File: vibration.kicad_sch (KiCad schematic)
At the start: 5 parts, among them J6 Conn_01x02, Q3 SS8050

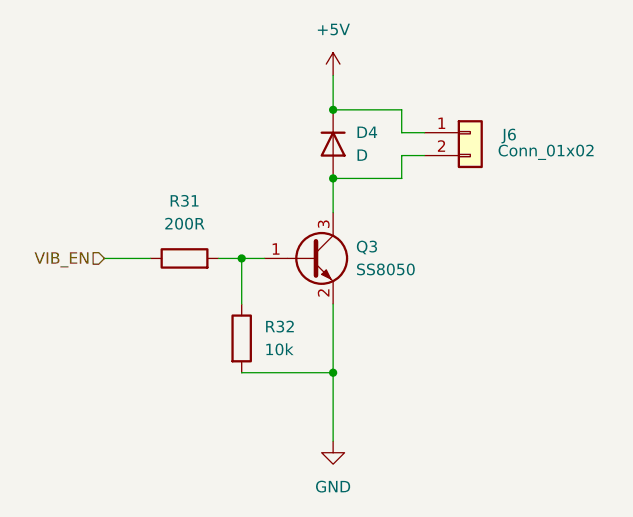
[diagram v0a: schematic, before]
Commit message: add SD card
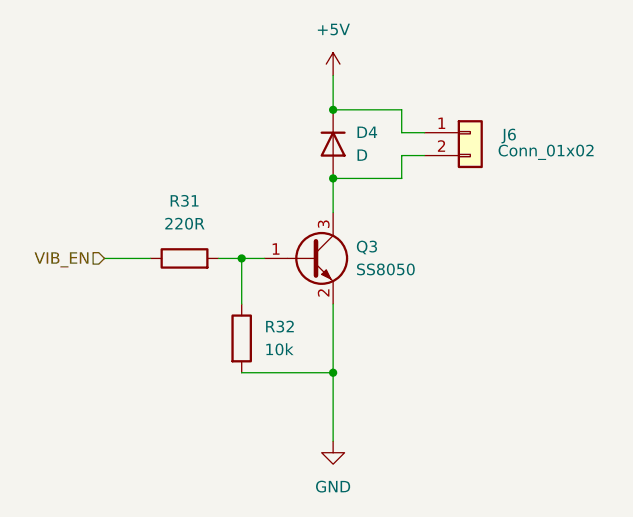
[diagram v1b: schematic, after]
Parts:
- D4: footprint (none) -> Diode_SMD:D_SMA; LCSC (none) -> C64982; Manufacturer (none) -> MDD(Microdiode Semiconductor); Manufacturer Part Number (none) -> B340A
- R31: value 200R -> 220R; footprint (none) -> Resistor_SMD:R_0603_1608Metric
- R32: footprint (none) -> Resistor_SMD:R_0603_1608Metric
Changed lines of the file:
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@@
 			)
 		)
-		(property "Footprint" ""
+		(property "Footprint" "Diode_SMD:D_SMA"
 			(at 132.08 74.93 0)
 			(effects
@@
 		)
 		(property "Sim.Pins" "1=K 2=A"
+			(at 132.08 74.93 0)
+			(effects
+				(font
+					(size 1.27 1.27)
+				)
+				(hide yes)
+			)
+		)
+		(property "LCSC" "C64982"
+			(at 132.08 74.93 0)
+			(effects
+				(font
+					(size 1.27 1.27)
+				)
+				(hide yes)
+			)
+		)
+		(property "Manufacturer" "MDD(Microdiode Semiconductor)"
+			(at 132.08 74.93 0)
+			(effects
+				(font
+					(size 1.27 1.27)
+				)
+				(hide yes)
+			)
+		)
+		(property "Manufacturer Part Number" "B340A"
 			(at 132.08 74.93 0)
 			(effects
@@
 			)
 		)
-		(property "Footprint" ""
+		(property "Footprint" "Resistor_SMD:R_0603_1608Metric"
 			(at 120.142 96.52 90)
 			(effects
@@
 			)
 		)
-		(property "Value" "200R"
+		(property "Value" "220R"
 			(at 115.57 83.82 90)
 			(effects
@@
 			)
 		)
-		(property "Footprint" ""
+		(property "Footprint" "Resistor_SMD:R_0603_1608Metric"
 			(at 115.57 89.408 90)
 			(effects

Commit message: small updates in component selection
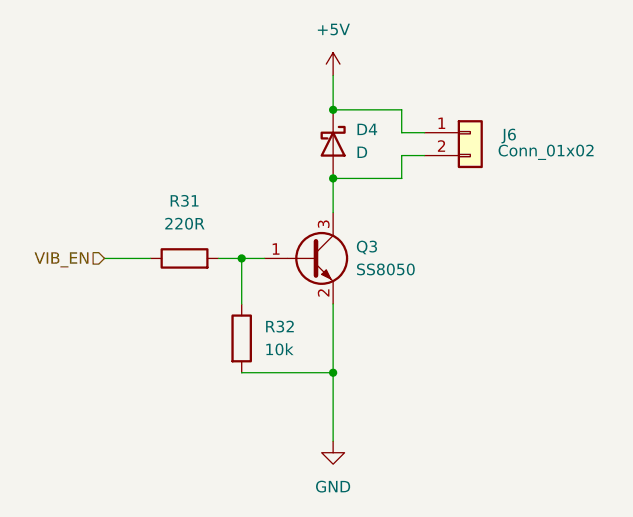
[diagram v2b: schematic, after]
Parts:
- D4: symbol Device:D -> Device:D_Schottky
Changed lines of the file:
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@@
 	)
 	(symbol
-		(lib_id "Device:D")
+		(lib_id "Device:D_Schottky")
 		(at 132.08 74.93 270)
 		(unit 1)
@@
 		(fields_autoplaced yes)
 		(property "Reference" "D4"
-			(at 134.62 73.6599 90)
+			(at 134.62 73.3424 90)
 			(effects
 				(font
@@
 		)
 		(property "Value" "D"
-			(at 134.62 76.1999 90)
+			(at 134.62 75.8824 90)
 			(effects
 				(font
@@
 			)
 		)
-		(property "Description" "Diode"
+		(property "Description" "Schottky diode"
 			(at 132.08 74.93 0)
 			(effects

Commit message: fix usb and add esd diodes, some other checks
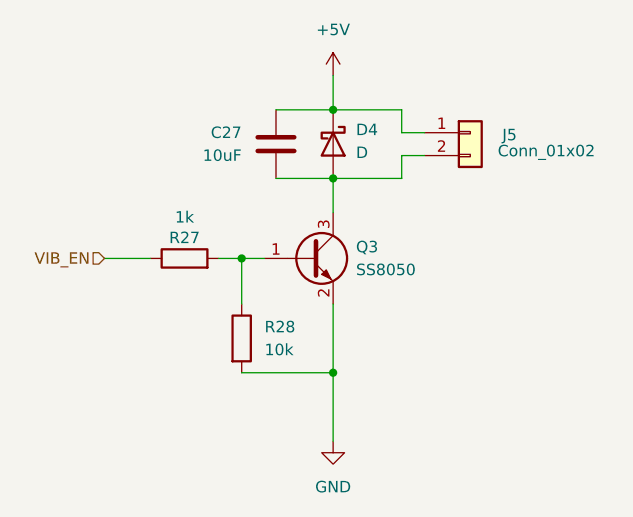
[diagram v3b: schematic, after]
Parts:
- removed R31: 220R, Resistor_SMD:R_0603_1608Metric, symbol Device:R
- added C27: 10uF, Capacitor_SMD:C_0603_1608Metric, symbol Device:C
- added R27: 1k, Resistor_SMD:R_0402_1005Metric, symbol Device:R
- renumbered J6 to J5, R32 to R28
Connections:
- net +5V: now also C27.1
- net VIB_EN: now also R27.1
- net at D4.2 (A), J5.2 (Pin_2), Q3.3 (C): now also C27.2
- net at Q3.1 (B), R28.1: now also R27.2
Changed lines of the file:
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@@
+	(wire
+		(pts
+			(xy 125.73 78.74) (xy 132.08 78.74)
+		)
+		(stroke
+			(width 0)
+			(type default)
+		)
+	)
 	(wire
 		(pts
@@
 		(pts
 			(xy 132.08 100.33) (xy 132.08 92.71)
+		)
+		(stroke
+			(width 0)
+			(type default)
+		)
+	)
+	(wire
+		(pts
+			(xy 125.73 71.12) (xy 132.08 71.12)
 		)
 		(stroke
@@
 		(on_board yes)
 		(dnp no)
-		(property "Reference" "J6"
+		(property "Reference" "J5"
 			(at 150.876 73.914 0)
 			(effects
@@
 			(project "gameboy"
 				(path "/f4643692-c319-40a7-82a2-3e775c0a417f/fa61dece-89ff-456c-a30f-6bfd2f1cc11c"
-					(reference "J6")
+					(reference "J5")
 					(unit 1)
 				)
@@
 	)
 	(symbol
+		(lib_id "Device:R")
+		(at 115.57 87.63 90)
+		(unit 1)
+		(exclude_from_sim no)
+		(in_bom yes)
+		(on_board yes)
+		(dnp no)
+		(property "Reference" "R27"
+			(at 115.57 85.344 90)
+			(effects
+				(font
+					(size 1.27 1.27)
+				)
+			)
+		)
+		(property "Value" "1k"
+			(at 115.57 83.058 90)
+			(effects
+				(font
+					(size 1.27 1.27)
+				)
+			)
+		)
+		(property "Footprint" "Resistor_SMD:R_0402_1005Metric"
+			(at 115.57 89.408 90)
+			(effects
+				(font
+					(size 1.27 1.27)
+				)
+				(hide yes)
+			)
+		)
+		(property "Datasheet" "~"
+			(at 115.57 87.63 0)
+			(effects
+				(font
+					(size 1.27 1.27)
+				)
+				(hide yes)
+			)
+		)
+		(property "Description" ""
+			(at 115.57 87.63 0)
+			(effects
+				(font
+					(size 1.27 1.27)
+				)
+			)
+		)
+		(pin "1"
+		)
+		(pin "2"
+		)
+		(instances
+			(project "gameboy"
+				(path "/f4643692-c319-40a7-82a2-3e775c0a417f/fa61dece-89ff-456c-a30f-6bfd2f1cc11c"
+					(reference "R27")
+					(unit 1)
+				)
+			)
+		)
+	)
+	(symbol
 		(lib_id "power:+5V")
 		(at 132.08 67.31 0)
@@
 		(dnp no)
 		(fields_autoplaced yes)
-		(property "Reference" "#PWR034"
+		(property "Reference" "#PWR033"
 			(at 132.08 71.12 0)
 			(effects
@@
 			(project ""
 				(path "/f4643692-c319-40a7-82a2-3e775c0a417f/fa61dece-89ff-456c-a30f-6bfd2f1cc11c"
-					(reference "#PWR034")
+					(reference "#PWR033")
+					(unit 1)
+				)
+			)
+		)
+	)
+	(symbol
+		(lib_id "Device:C")
+		(at 125.73 74.93 0)
+		(mirror y)
+		(unit 1)
+		(exclude_from_sim no)
+		(in_bom yes)
+		(on_board yes)
+		(dnp no)
+		(property "Reference" "C27"
+			(at 121.92 73.6599 0)
+			(effects
+				(font
+					(size 1.27 1.27)
+				)
+				(justify left)
+			)
+		)
+		(property "Value" "10uF"
+			(at 121.92 76.1999 0)
+			(effects
+				(font
+					(size 1.27 1.27)
+				)
+				(justify left)
+			)
+		)
+		(property "Footprint" "Capacitor_SMD:C_0603_1608Metric"
+			(at 124.7648 78.74 0)
+			(effects
+				(font
+					(size 1.27 1.27)
+				)
+				(hide yes)
+			)
+		)
+		(property "Datasheet" "~"
+			(at 125.73 74.93 0)
+			(effects
+				(font
+					(size 1.27 1.27)
+				)
+				(hide yes)
+			)
+		)
+		(property "Description" "Unpolarized capacitor"
+			(at 125.73 74.93 0)
+			(effects
+				(font
+					(size 1.27 1.27)
+				)
+				(hide yes)
+			)
+		)
+		(property "LCSC" ""
+			(at 125.73 74.93 0)
+			(effects
+				(font
+					(size 1.27 1.27)
+				)
+				(hide yes)
+			)
+		)
+		(property "Manufacturer" ""
+			(at 125.73 74.93 0)
+			(effects
+				(font
+					(size 1.27 1.27)
+				)
+				(hide yes)
+			)
+		)
+		(property "Manufacturer Part Number" ""
+			(at 125.73 74.93 0)
+			(effects
+				(font
+					(size 1.27 1.27)
+				)
+				(hide yes)
+			)
+		)
+		(pin "2"
+		)
+		(pin "1"
+		)
+		(instances
+			(project "gameboy"
+				(path "/f4643692-c319-40a7-82a2-3e775c0a417f/fa61dece-89ff-456c-a30f-6bfd2f1cc11c"
+					(reference "C27")
 					(unit 1)
 				)
@@
 		(dnp no)
 		(fields_autoplaced yes)
-		(property "Reference" "#PWR035"
+		(property "Reference" "#PWR034"
 			(at 132.08 114.3 0)
 			(effects
@@
 			(project ""
 				(path "/f4643692-c319-40a7-82a2-3e775c0a417f/fa61dece-89ff-456c-a30f-6bfd2f1cc11c"
-					(reference "#PWR035")
+					(reference "#PWR034")
 					(unit 1)
 				)
@@
 		(dnp no)
 		(fields_autoplaced yes)
-		(property "Reference" "R32"
+		(property "Reference" "R28"
 			(at 124.46 95.2499 0)
 			(effects
@@
 			(project ""
 				(path "/f4643692-c319-40a7-82a2-3e775c0a417f/fa61dece-89ff-456c-a30f-6bfd2f1cc11c"
-					(reference "R32")
+					(reference "R28")
 					(unit 1)
 				)
-			)
-		)
-	)
-	(symbol
-		(lib_id "Device:R")
-		(at 115.57 87.63 90)
-		(unit 1)
-		(exclude_from_sim no)
-		(in_bom yes)
-		(on_board yes)
-		(dnp no)
-		(fields_autoplaced yes)
-		(property "Reference" "R31"
-			(at 115.57 81.28 90)
-			(effects
-				(font
-					(size 1.27 1.27)
-				)
-			)
-		)
-		(property "Value" "220R"
-			(at 115.57 83.82 90)
-			(effects
-				(font
-					(size 1.27 1.27)
-				)
-			)
-		)
-		(property "Footprint" "Resistor_SMD:R_0603_1608Metric"
-			(at 115.57 89.408 90)
-			(effects
-				(font
-					(size 1.27 1.27)
-				)
-				(hide yes)
-			)
-		)
-		(property "Datasheet" "~"
-			(at 115.57 87.63 0)
-			(effects
-				(font
-					(size 1.27 1.27)
-				)
-				(hide yes)
-			)
-		)
-		(property "Description" "Resistor"
-			(at 115.57 87.63 0)
-			(effects
-				(font
-					(size 1.27 1.27)
-				)
-				(hide yes)
-			)
-		)
-		(property "LCSC" ""
-			(at 115.57 87.63 0)
-			(effects
-				(font
-					(size 1.27 1.27)
-				)
-				(hide yes)
-			)
-		)
-		(property "Manufacturer" ""
-			(at 115.57 87.63 0)
-			(effects
-				(font
-					(size 1.27 1.27)
-				)
-				(hide yes)
-			)
-		)
-		(property "Manufacturer Part Number" ""
-			(at 115.57 87.63 0)
-			(effects
-				(font
-					(size 1.27 1.27)
-				)
-				(hide yes)
-			)
-		)
-		(pin "1"
-		)
-		(pin "2"
-		)
-		(instances
-			(project ""
-				(path "/f4643692-c319-40a7-82a2-3e775c0a417f/fa61dece-89ff-456c-a30f-6bfd2f1cc11c"
-					(reference "R31")
-					(unit 1)
-				)

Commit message: whole bunch of layout done
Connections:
- net +5V renamed VDC
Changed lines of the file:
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@@
-	)
-	(symbol
-		(lib_id "power:+5V")
-		(at 132.08 67.31 0)
-		(unit 1)
-		(exclude_from_sim no)
-		(in_bom yes)
-		(on_board yes)
-		(dnp no)
-		(fields_autoplaced yes)
-		(property "Reference" "#PWR033"
-			(at 132.08 71.12 0)
-			(effects
-				(font
-					(size 1.27 1.27)
-				)
-				(hide yes)
-			)
-		)
-		(property "Value" "+5V"
-			(at 132.08 62.23 0)
-			(effects
-				(font
-					(size 1.27 1.27)
-				)
-			)
-		)
-		(property "Footprint" ""
-			(at 132.08 67.31 0)
-			(effects
-				(font
-					(size 1.27 1.27)
-				)
-				(hide yes)
-			)
-		)
-		(property "Datasheet" ""
-			(at 132.08 67.31 0)
-			(effects
-				(font
-					(size 1.27 1.27)
-				)
-				(hide yes)
-			)
-		)
-		(property "Description" "Power symbol creates a global label with name \"+5V\""
-			(at 132.08 67.31 0)
-			(effects
-				(font
-					(size 1.27 1.27)
-				)
-				(hide yes)
-			)
-		)
-		(pin "1"
-		)
-		(instances
-			(project ""
-				(path "/f4643692-c319-40a7-82a2-3e775c0a417f/fa61dece-89ff-456c-a30f-6bfd2f1cc11c"
-					(reference "#PWR033")
-					(unit 1)
-				)
-			)
-		)
 	)
 	(symbol
@@
 					(unit 1)
 				)
+			)
+		)
+	)
+	(symbol
+		(lib_id "power:VDC")
+		(at 132.08 67.31 0)
+		(unit 1)
+		(exclude_from_sim no)
+		(in_bom yes)
+		(on_board yes)
+		(dnp no)
+		(fields_autoplaced yes)
+		(property "Reference" "#PWR026"
+			(at 132.08 71.12 0)
+			(effects
+				(font
+					(size 1.27 1.27)
+				)
+				(hide yes)
+			)
+		)
+		(property "Value" "VDC"
+			(at 132.08 62.23 0)
+			(effects
+				(font
+					(size 1.27 1.27)
+				)
+			)
+		)
+		(property "Footprint" ""
+			(at 132.08 67.31 0)
+			(effects
+				(font
+					(size 1.27 1.27)
+				)
+				(hide yes)
+			)
+		)
+		(property "Datasheet" ""
+			(at 132.08 67.31 0)
+			(effects
+				(font
+					(size 1.27 1.27)
+				)
+				(hide yes)
+			)
+		)
+		(property "Description" "Power symbol creates a global label with name \"VDC\""
+			(at 132.08 67.31 0)
+			(effects
+				(font
+					(size 1.27 1.27)
+				)
+				(hide yes)
+			)
+		)
+		(pin "1"
+		)
+		(instances
+			(project ""
+				(path "/f4643692-c319-40a7-82a2-3e775c0a417f/fa61dece-89ff-456c-a30f-6bfd2f1cc11c"
+					(reference "#PWR026")
+					(unit 1)
+				)

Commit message: more routing
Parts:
- J5: footprint Connector_JST:JST_PH_B2B-PH-K_1x02_P2.00mm_Vertical -> Connector_JST:JST_PH_S2B-PH-SM4-TB_1x02-1MP_P2.00mm_Horizontal; LCSC C131337 -> C295747; Manufacturer Part Number B2B-PH-K-S(LF)(SN) -> S2B-PH-SM4-TB(LF)(SN)
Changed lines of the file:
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@@
-	)
-	(symbol
-		(lib_id "Connector_Generic:Conn_01x02")
-		(at 147.32 73.66 0)
-		(unit 1)
-		(exclude_from_sim no)
-		(in_bom yes)
-		(on_board yes)
-		(dnp no)
-		(property "Reference" "J5"
-			(at 150.876 73.914 0)
-			(effects
-				(font
-					(size 1.27 1.27)
-				)
-				(justify left)
-			)
-		)
-		(property "Value" "Conn_01x02"
-			(at 150.368 75.692 0)
-			(effects
-				(font
-					(size 1.27 1.27)
-				)
-				(justify left)
-			)
-		)
-		(property "Footprint" "Connector_JST:JST_PH_B2B-PH-K_1x02_P2.00mm_Vertical"
-			(at 147.32 73.66 0)
-			(effects
-				(font
-					(size 1.27 1.27)
-				)
-				(hide yes)
-			)
-		)
-		(property "Datasheet" "~"
-			(at 147.32 73.66 0)
-			(effects
-				(font
-					(size 1.27 1.27)
-				)
-				(hide yes)
-			)
-		)
-		(property "Description" "Generic connector, single row, 01x02, script generated (kicad-library-utils/schlib/autogen/connector/)"
-			(at 147.32 73.66 0)
-			(effects
-				(font
-					(size 1.27 1.27)
-				)
-				(hide yes)
-			)
-		)
-		(property "LCSC" "C131337"
-			(at 147.32 73.66 0)
-			(effects
-				(font
-					(size 1.27 1.27)
-				)
-				(hide yes)
-			)
-		)
-		(property "Manufacturer" "JST"
-			(at 147.32 73.66 0)
-			(effects
-				(font
-					(size 1.27 1.27)
-				)
-				(hide yes)
-			)
-		)
-		(property "Manufacturer Part Number" "B2B-PH-K-S(LF)(SN)"
-			(at 147.32 73.66 0)
-			(effects
-				(font
-					(size 1.27 1.27)
-				)
-				(hide yes)
-			)
-		)
-		(pin "2"
-		)
-		(pin "1"
-		)
-		(instances
-			(project "gameboy"
-				(path "/f4643692-c319-40a7-82a2-3e775c0a417f/fa61dece-89ff-456c-a30f-6bfd2f1cc11c"
-					(reference "J5")
-					(unit 1)
-				)
-			)
-		)
 	)
 	(symbol
@@
 					(unit 1)
 				)
+			)
+		)
+	)
+	(symbol
+		(lib_id "Connector_Generic:Conn_01x02")
+		(at 147.32 73.66 0)
+		(unit 1)
+		(exclude_from_sim no)
+		(in_bom yes)
+		(on_board yes)
+		(dnp no)
+		(property "Reference" "J5"
+			(at 150.876 73.914 0)
+			(effects
+				(font
+					(size 1.27 1.27)
+				)
+				(justify left)
+			)
+		)
+		(property "Value" "Conn_01x02"
+			(at 150.368 75.692 0)
+			(effects
+				(font
+					(size 1.27 1.27)
+				)
+				(justify left)
+			)
+		)
+		(property "Footprint" "Connector_JST:JST_PH_S2B-PH-SM4-TB_1x02-1MP_P2.00mm_Horizontal"
+			(at 147.32 73.66 0)
+			(effects
+				(font
+					(size 1.27 1.27)
+				)
+				(hide yes)
+			)
+		)
+		(property "Datasheet" "~"
+			(at 147.32 73.66 0)
+			(effects
+				(font
+					(size 1.27 1.27)
+				)
+				(hide yes)
+			)
+		)
+		(property "Description" "Generic connector, single row, 01x02, script generated (kicad-library-utils/schlib/autogen/connector/)"
+			(at 147.32 73.66 0)
+			(effects
+				(font
+					(size 1.27 1.27)
+				)
+				(hide yes)
+			)
+		)
+		(property "LCSC" "C295747"
+			(at 147.32 73.66 0)
+			(effects
+				(font
+					(size 1.27 1.27)
+				)
+				(hide yes)
+			)
+		)
+		(property "Manufacturer" "JST"
+			(at 147.32 73.66 0)
+			(effects
+				(font
+					(size 1.27 1.27)
+				)
+				(hide yes)
+			)
+		)
+		(property "Manufacturer Part Number" "S2B-PH-SM4-TB(LF)(SN)"
+			(at 147.32 73.66 0)
+			(effects
+				(font
+					(size 1.27 1.27)
+				)
+				(hide yes)
+			)
+		)
+		(pin "2"
+		)
+		(pin "1"
+		)
+		(instances
+			(project "gameboy"
+				(path "/f4643692-c319-40a7-82a2-3e775c0a417f/fa61dece-89ff-456c-a30f-6bfd2f1cc11c"
+					(reference "J5")
+					(unit 1)
+				)

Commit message: route vibration and speaker
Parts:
- R27: footprint Resistor_SMD:R_0402_1005Metric -> Resistor_SMD:R_0603_1608Metric
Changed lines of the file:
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@@
 			)
 		)
-		(property "Footprint" "Resistor_SMD:R_0402_1005Metric"
+		(property "Footprint" "Resistor_SMD:R_0603_1608Metric"
 			(at 115.57 89.408 90)
 			(effects
@@
 			)
 		)
+		(property "LCSC" ""
+			(at 115.57 87.63 0)
+			(effects
+				(font
+					(size 1.27 1.27)
+				)
+				(hide yes)
+			)
+		)
+		(property "Manufacturer" ""
+			(at 115.57 87.63 0)
+			(effects
+				(font
+					(size 1.27 1.27)
+				)
+				(hide yes)
+			)
+		)
+		(property "Manufacturer Part Number" ""
+			(at 115.57 87.63 0)
+			(effects
+				(font
+					(size 1.27 1.27)
+				)
+				(hide yes)
+			)
+		)

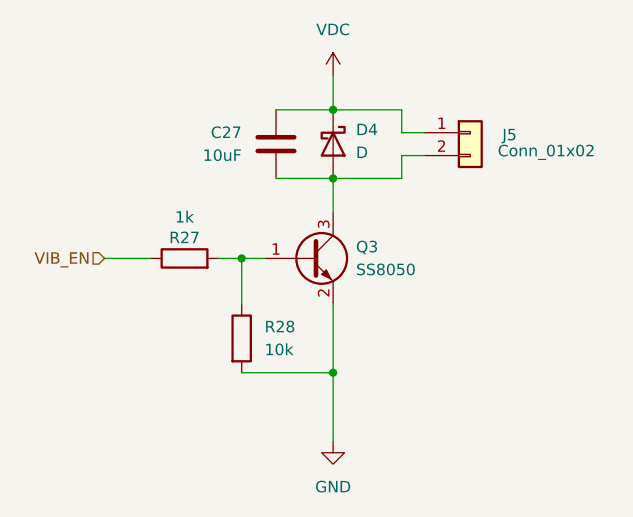
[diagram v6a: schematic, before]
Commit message: add silkscreen, optimize layout and replace sd card peripheral
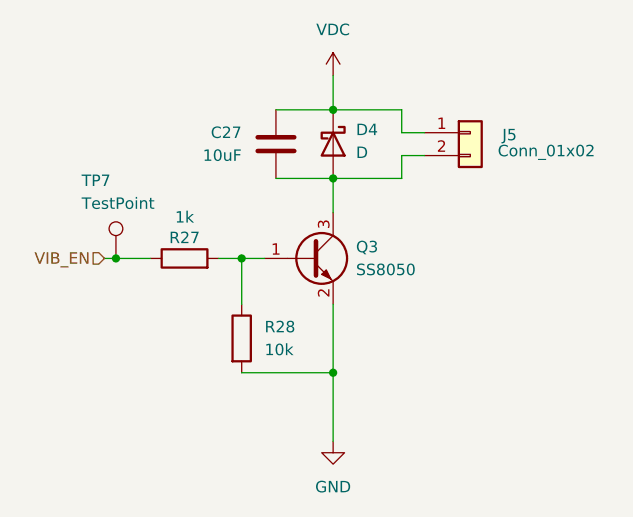
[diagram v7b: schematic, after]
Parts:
- added TP7: TestPoint, TestPoint:TestPoint_Pad_D1.0mm, symbol Connector:TestPoint
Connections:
- net VIB_EN: now also TP7.1
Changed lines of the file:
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@@
+	)
+	(junction
+		(at 107.95 87.63)
+		(diameter 0)
+		(color 0 0 0 0)
 	)
 	(junction
@@
 	(wire
 		(pts
+			(xy 106.68 87.63) (xy 107.95 87.63)
+		)
+		(stroke
+			(width 0)
+			(type default)
+		)
+	)
+	(wire
+		(pts
 			(xy 139.7 78.74) (xy 132.08 78.74)
 		)
@@
 	(wire
 		(pts
+			(xy 107.95 87.63) (xy 111.76 87.63)
+		)
+		(stroke
+			(width 0)
+			(type default)
+		)
+	)
+	(wire
+		(pts
 			(xy 132.08 67.31) (xy 132.08 71.12)
-		)
-		(stroke
-			(width 0)
-			(type default)
-		)
-	)
-	(wire
-		(pts
-			(xy 106.68 87.63) (xy 111.76 87.63)
 		)
 		(stroke
@@
 					(unit 1)
 				)
+			)
+		)
+	)
+	(symbol
+		(lib_id "Connector:TestPoint")
+		(at 107.95 87.63 0)
+		(unit 1)
+		(exclude_from_sim no)
+		(in_bom yes)
+		(on_board yes)
+		(dnp no)
+		(property "Reference" "TP7"
+			(at 104.14 78.994 0)
+			(effects
+				(font
+					(size 1.27 1.27)
+				)
+				(justify left)
+			)
+		)
+		(property "Value" "TestPoint"
+			(at 104.14 81.534 0)
+			(effects
+				(font
+					(size 1.27 1.27)
+				)
+				(justify left)
+			)
+		)
+		(property "Footprint" "TestPoint:TestPoint_Pad_D1.0mm"
+			(at 113.03 87.63 0)
+			(effects
+				(font
+					(size 1.27 1.27)
+				)
+				(hide yes)
+			)
+		)
+		(property "Datasheet" "~"
+			(at 113.03 87.63 0)
+			(effects
+				(font
+					(size 1.27 1.27)
+				)
+				(hide yes)
+			)
+		)
+		(property "Description" "test point"
+			(at 107.95 87.63 0)
+			(effects
+				(font
+					(size 1.27 1.27)
+				)
+				(hide yes)
+			)
+		)
+		(property "LCSC" ""
+			(at 107.95 87.63 0)
+			(effects
+				(font
+					(size 1.27 1.27)
+				)
+				(hide yes)
+			)
+		)
+		(property "Manufacturer" ""
+			(at 107.95 87.63 0)
+			(effects
+				(font
+					(size 1.27 1.27)
+				)
+				(hide yes)
+			)
+		)
+		(property "Manufacturer Part Number" ""
+			(at 107.95 87.63 0)
+			(effects
+				(font
+					(size 1.27 1.27)
+				)
+				(hide yes)
+			)
+		)
+		(pin "1"
+		)
+		(instances
+			(project "gameboy"
+				(path "/f4643692-c319-40a7-82a2-3e775c0a417f/fa61dece-89ff-456c-a30f-6bfd2f1cc11c"
+					(reference "TP7")
+					(unit 1)
+				)
